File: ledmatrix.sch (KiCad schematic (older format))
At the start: 77 parts, among them CN2 100nF, CN3 100nF, CN4 100nF, CN5 100nF, U58 sled1735

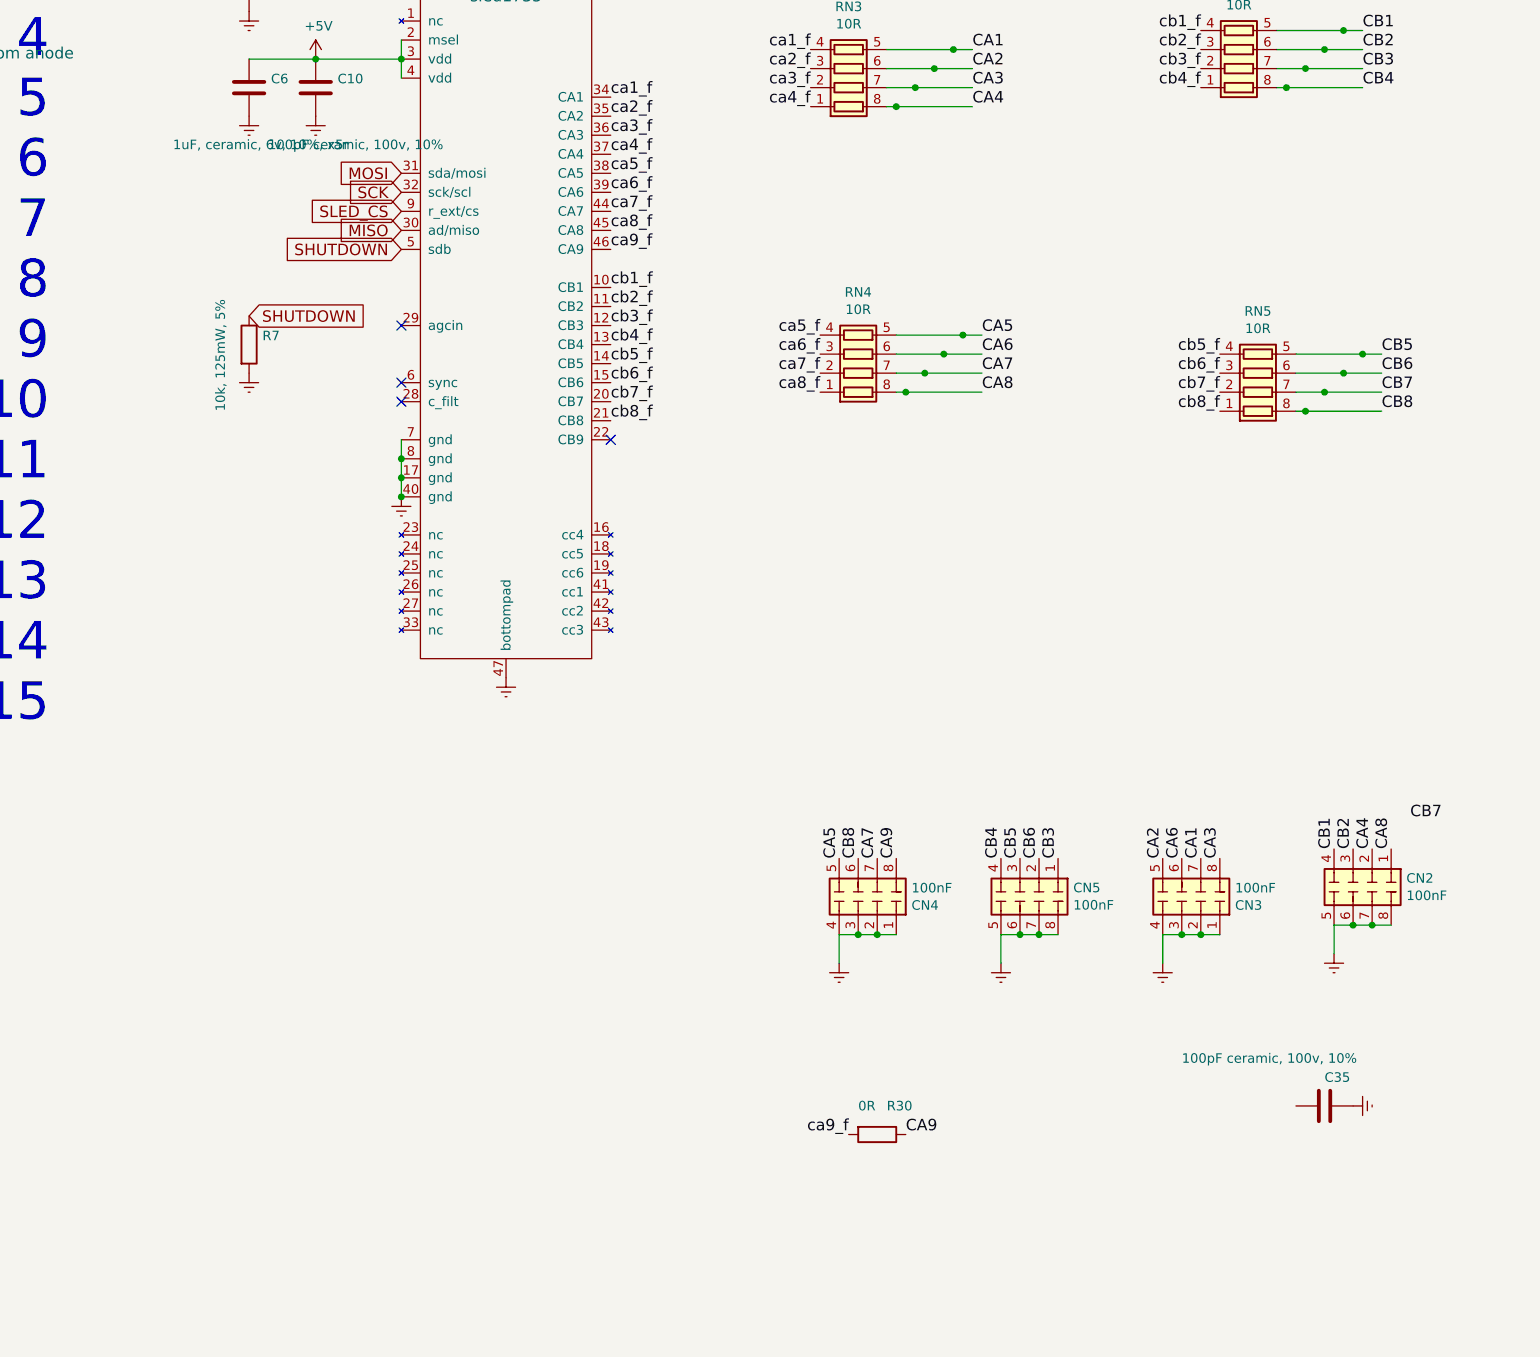
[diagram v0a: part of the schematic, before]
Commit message: still to route: spi, filtered rows, i2c filtering
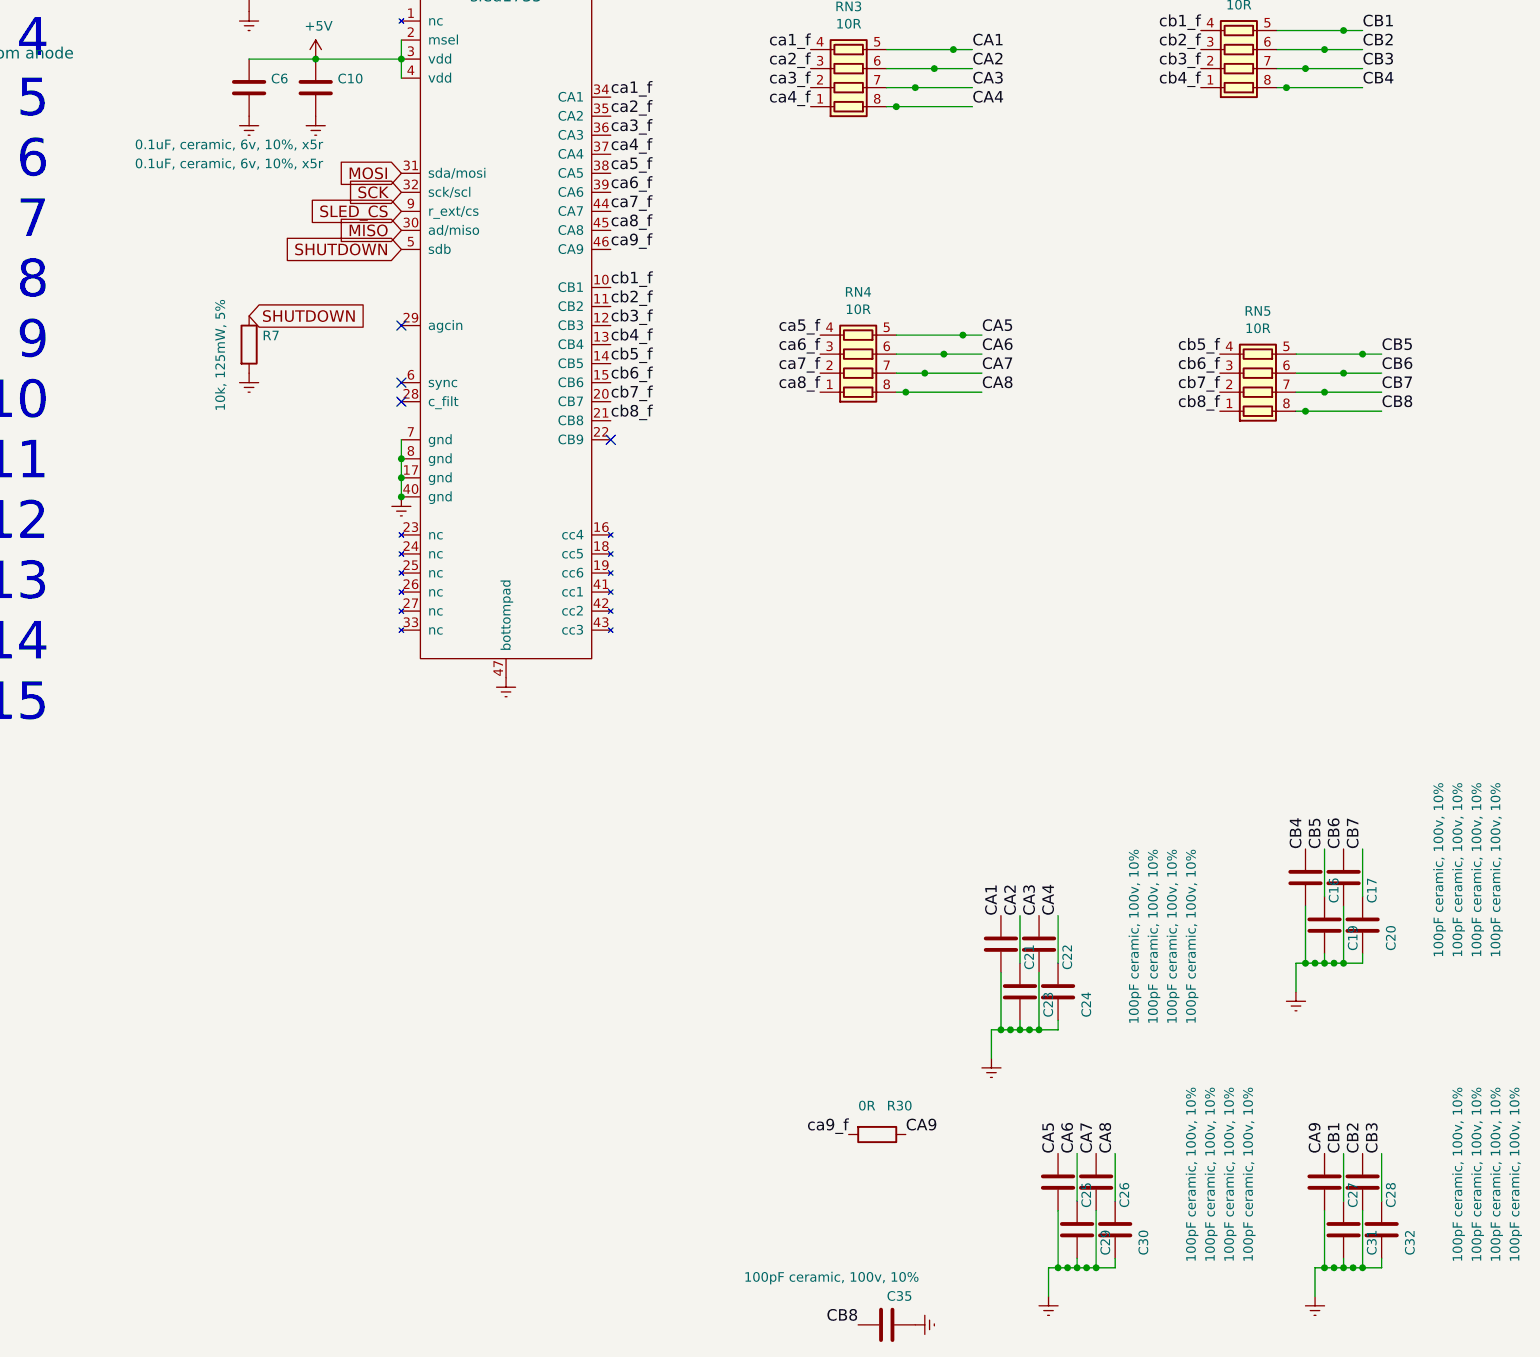
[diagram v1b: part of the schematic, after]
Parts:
- removed CN2, CN3, CN4, CN5: 100nF, raise_fp:R_Array_Convex_4x0402, symbol C_Pack04
- added C16, C17, C19, C20, C21, C22, C23, C24, C25, C26, C27, C28, C29, C30, C31, C32: 100pF ceramic, 100v, 10%, raise_fp:C_0603, symbol C
- C10: value 100pF ceramic, 100v, 10% -> 0.1uF, ceramic, 6v, 10%, x5r; farnell # 2821263 -> 1865556
- C6: value 1uF, ceramic, 6v, 10%, x5r -> 0.1uF, ceramic, 6v, 10%, x5r
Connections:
- wire segments 80 -> 104
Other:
- moved on the sheet: C35

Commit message: farnell values for new cap values
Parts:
- C10, C6: value 0.1uF, ceramic, 6v, 10%, x5r -> 0.1uF, ceramic, 10v, 10%, x5r; farnell # 1865556 -> 2896426
- C16, C17, C19, C20, C21, C22, C23, C24, C25, C26, C27, C28, C29, C30, C31, C32, C35: value 100pF ceramic, 100v, 10% -> 1nF ceramic, 100v, 10%; farnell # 2821263 -> 2896415
- R30: value 0R -> 10R
- RN2, RN3, RN4, RN5: farnell # (none) -> 2060029
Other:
- moved on the sheet: C16, C17, C19, C20, C21, C22, C23, C24, C25, C26, C27, C28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

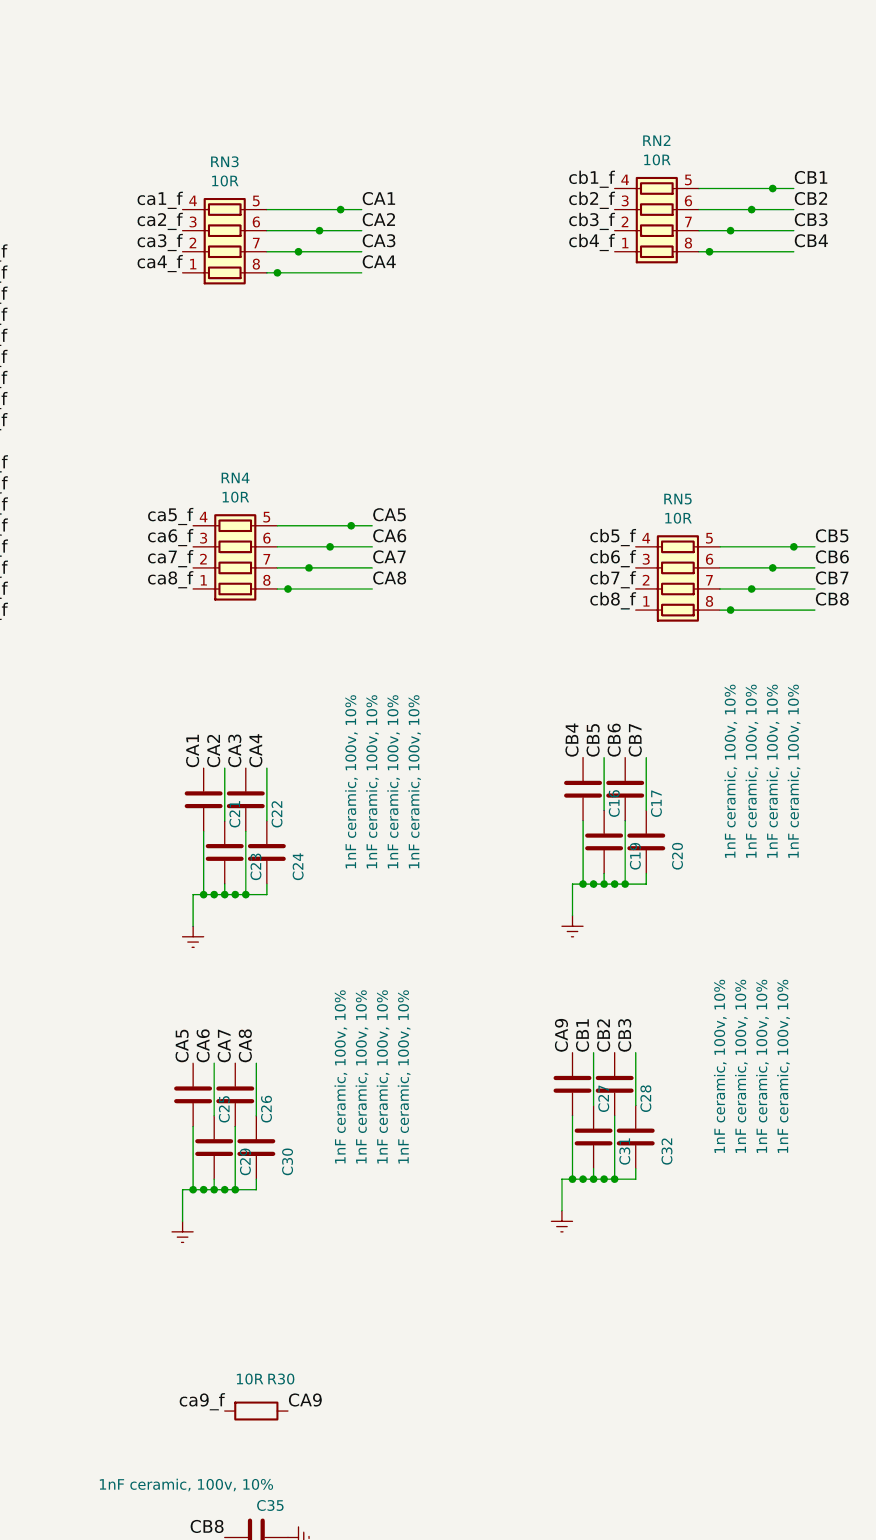
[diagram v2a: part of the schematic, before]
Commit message: updated cap values, fixed mask on sled1735
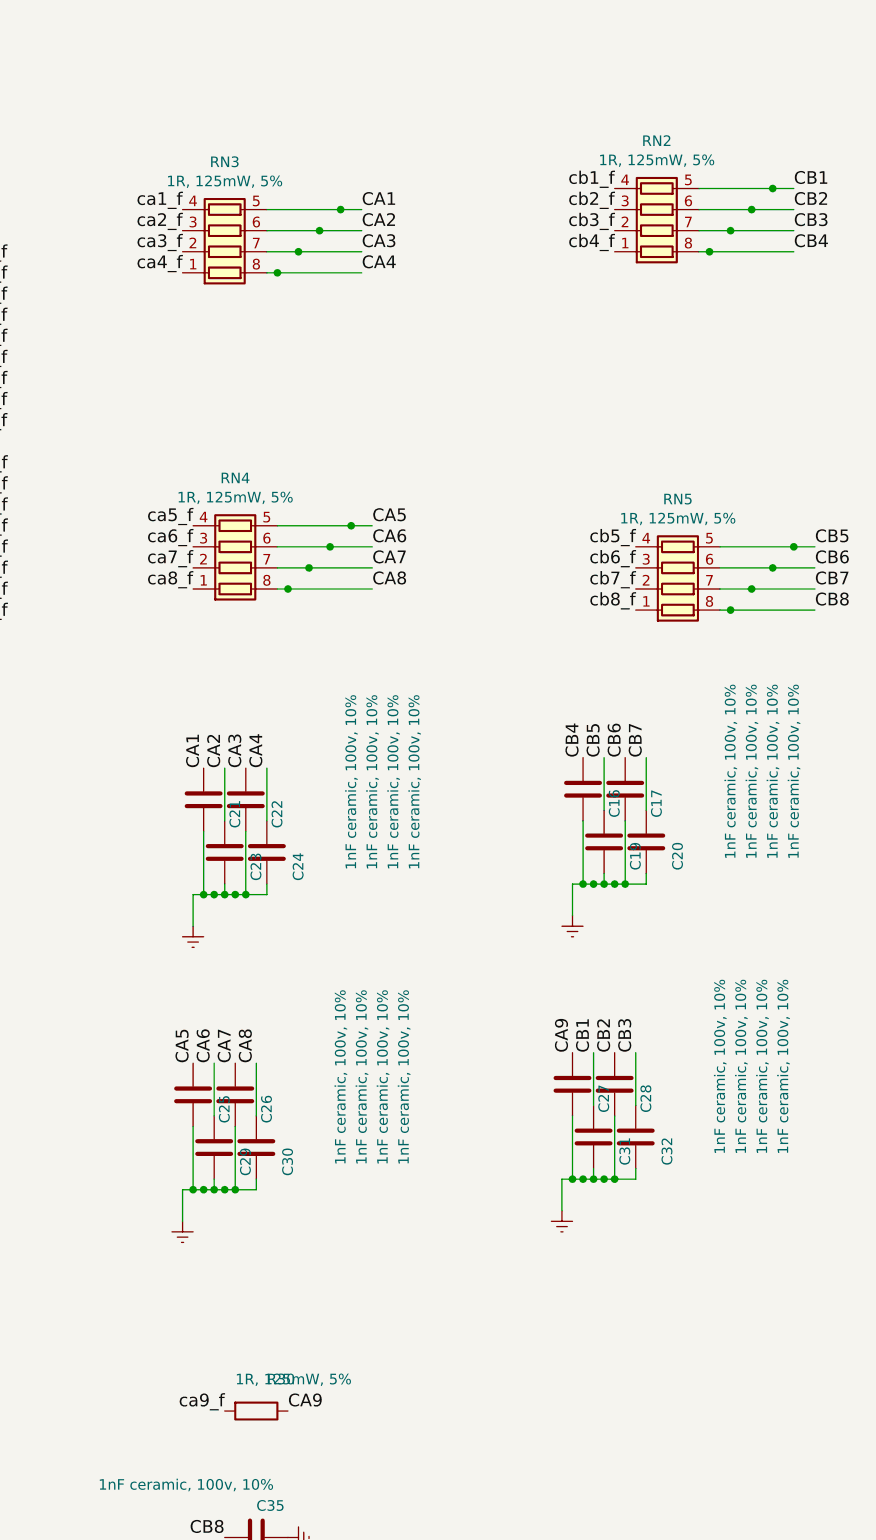
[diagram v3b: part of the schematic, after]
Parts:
- R30, RN2, RN3, RN4, RN5: value 10R -> 1R, 125mW, 5%
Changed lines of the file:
@@
 P 12550 7600
 F 0 "R30" V 12400 7650 50  0000 L CNN
-F 1 "10R" V 12400 7500 50  0000 L CNN
+F 1 "1R,  125mW, 5%" V 12400 7500 50  0000 L CNN
 F 2 "raise_fp:R_0603" V 12480 7600 50  0001 C CNN
 F 3 "" H 12550 7600 50  0000 C CNN
@@
 P 12400 2000
 F 0 "RN3" V 12725 2000 50  0000 C CNN
-F 1 "10R" V 12634 2000 50  0000 C CNN
+F 1 "1R, 125mW, 5%" V 12634 2000 50  0000 C CNN
 F 2 "raise_fp:R_Array_Convex_4x0402" V 12675 2000 50  0001 C CNN
 F 3 "" H 12400 2000 50  0001 C CNN
@@
 P 12450 3500
 F 0 "RN4" V 12775 3500 50  0000 C CNN
-F 1 "10R" V 12684 3500 50  0000 C CNN
+F 1 "1R, 125mW, 5%" V 12684 3500 50  0000 C CNN
 F 2 "raise_fp:R_Array_Convex_4x0402" V 12725 3500 50  0001 C CNN
 F 3 "" H 12450 3500 50  0001 C CNN
@@
 P 14450 1900
 F 0 "RN2" V 14775 1900 50  0000 C CNN
-F 1 "10R" V 14684 1900 50  0000 C CNN
+F 1 "1R, 125mW, 5%" V 14684 1900 50  0000 C CNN
 F 2 "raise_fp:R_Array_Convex_4x0402" V 14725 1900 50  0001 C CNN
 F 3 "" H 14450 1900 50  0001 C CNN
@@
 P 14550 3600
 F 0 "RN5" V 14875 3600 50  0000 C CNN
-F 1 "10R" V 14784 3600 50  0000 C CNN
+F 1 "1R, 125mW, 5%" V 14784 3600 50  0000 C CNN
 F 2 "raise_fp:R_Array_Convex_4x0402" V 14825 3600 50  0001 C CNN
 F 3 "" H 14550 3600 50  0001 C CNN
